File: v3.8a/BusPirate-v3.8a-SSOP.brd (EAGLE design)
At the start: 50 x 50 mm, 43 parts, among them IC1 PIC24FJ64GA002, IC3 4066, IC4 IC_FT230X-SSOP-16, J1 CON-USB-F-MINI-B

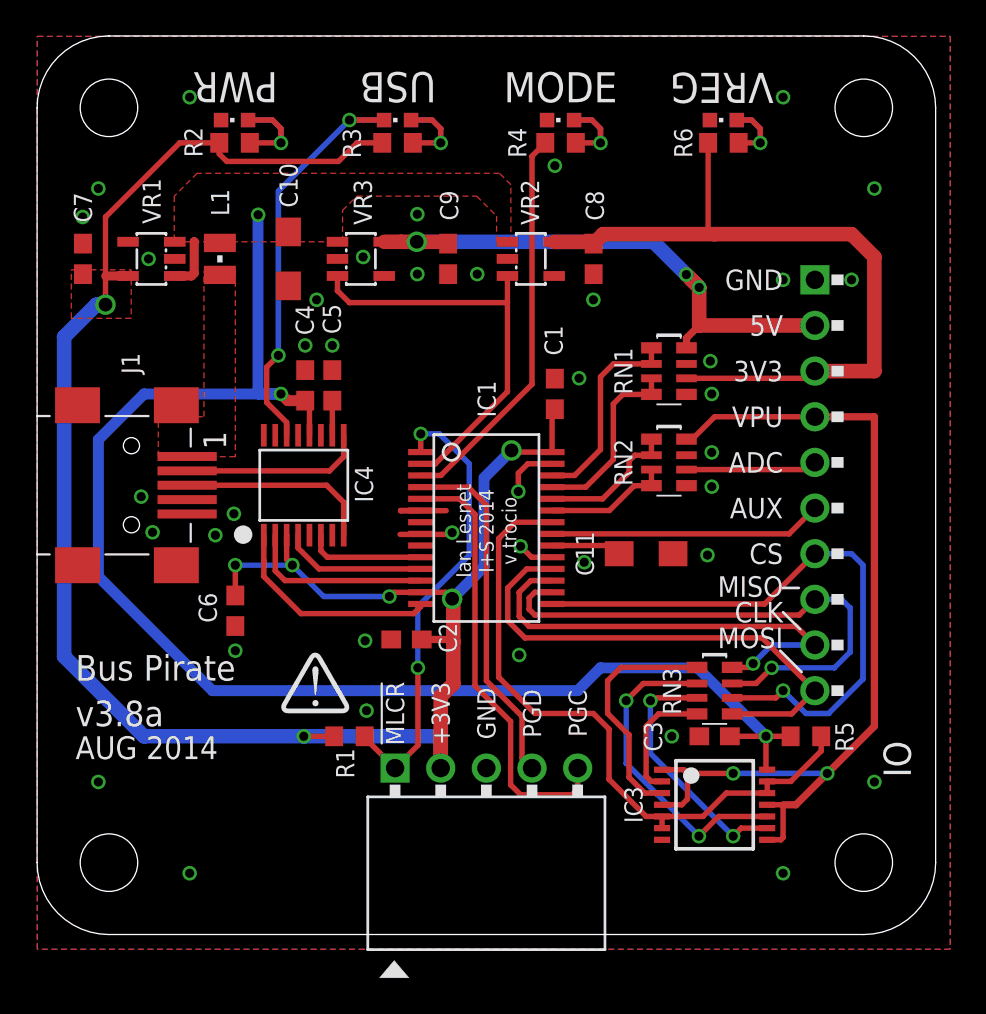
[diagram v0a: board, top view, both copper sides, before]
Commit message: -replaced SMD version for the IO and ICSP header -fixed over hang distance of header including USB connector to 1.25mm -gerber generated
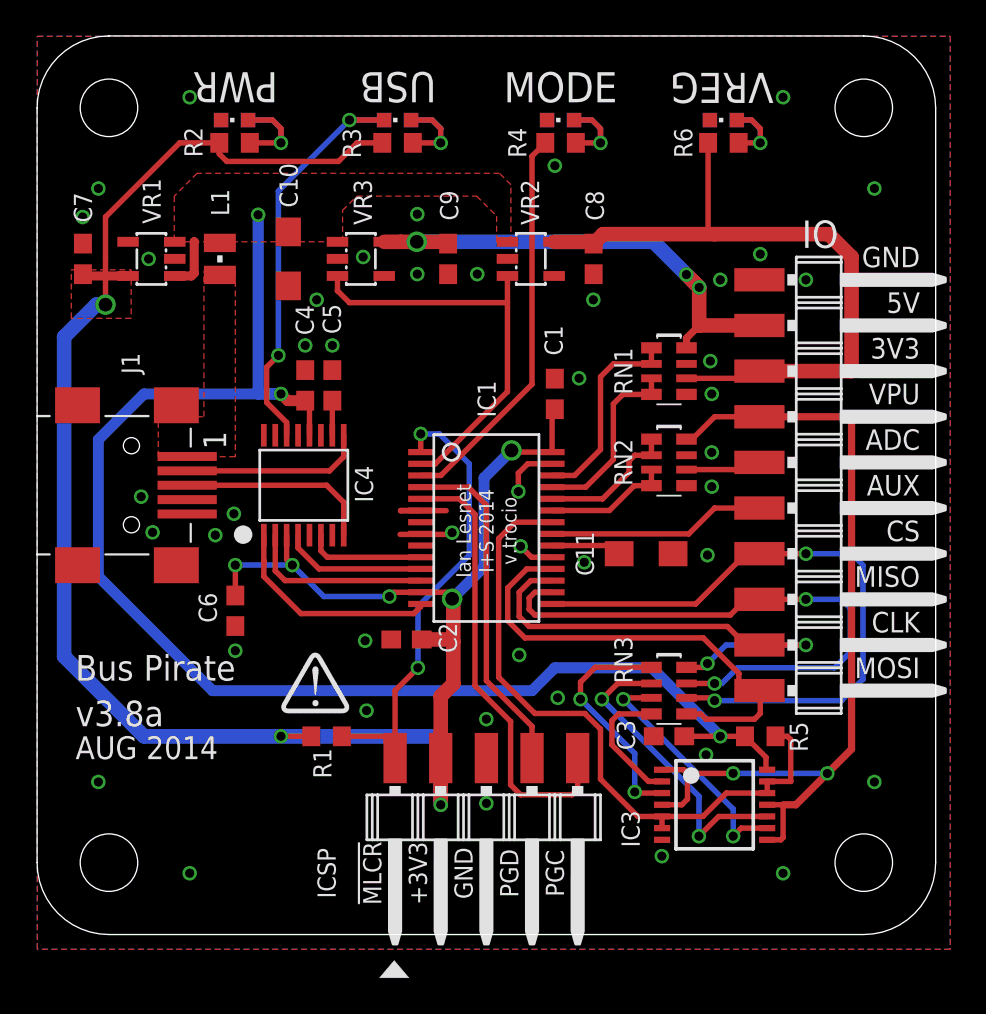
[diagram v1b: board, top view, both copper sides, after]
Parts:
- ICSP: value CON_HEADER_1X05-PTH_RIGHT_ANGLED_B -> CON_HEADER_1X05-SMD_RIGHT_ANGLED_MALE_B; device dp_devices.v6:M1X5_FEMALE_RIGHT_ANGLED_PTH_B -> dp_devices.v6:M1X5_MALE_RIGHT_ANGLED_SMD_B
- IO: value CON_HEADER_1X10-RIGHT_ANGLED_PTH -> CON_HEADER_1X10-_RIGHTANGLED_SMD; device dp_devices.v6:M1X10_FEMALE_RIGHT_ANGLED_PTH -> dp_devices.v6:M1X10_MALE_RIGHT_ANGLED_SMD
- moved IO 5.64 mm to (43.9, 25.4)
- moved ICSP 3.11 mm to (25.4, 6.92)
- moved C3 2.54 mm to (35.6, 11.4)
- moved R5 2.54 mm to (40.6, 11.4)
- moved RN3 2.54 mm to (35.6, 14.0)
- moved R1 1.27 mm to (16.5, 11.4)
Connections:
- net V+ renamed VUSB
- net VCC renamed +3V3
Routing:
- net +3V3: track 114.4 -> 120.7 mm, vias 7 -> 8
- net ADC: track 7.31 -> 4.22 mm
- net AUX1: track 15.2 -> 12.1 mm
- net SWV50: track 32.3 -> 29.2 mm
- net MISO: track 30.3 -> 32.9 mm, vias 1 -> 2
- net SWV33: track 41.0 -> 38.5 mm
- net VUSB: track 83.7 -> 81.7 mm
- net MOSI: track 28.6 -> 26.7 mm
- net VEXTERN: track 51.0 -> 49.2 mm
- net CS: track 33.8 -> 35.4 mm, vias 1 -> 2
- net CLK: track 25.7 -> 27.2 mm, vias 1 -> 2
- net MCLR: track 25.5 -> 26.7 mm
- net N$4: track 17.8 -> 17.2 mm
- net PGD: track 19.8 -> 19.2 mm
- net PGC: track 24.5 -> 25.1 mm
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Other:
- board text added: "ICSP"

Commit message: board update: -changed ICSP header to 6pins, spare pin not connected -moved all LEDs a little to the right for even space
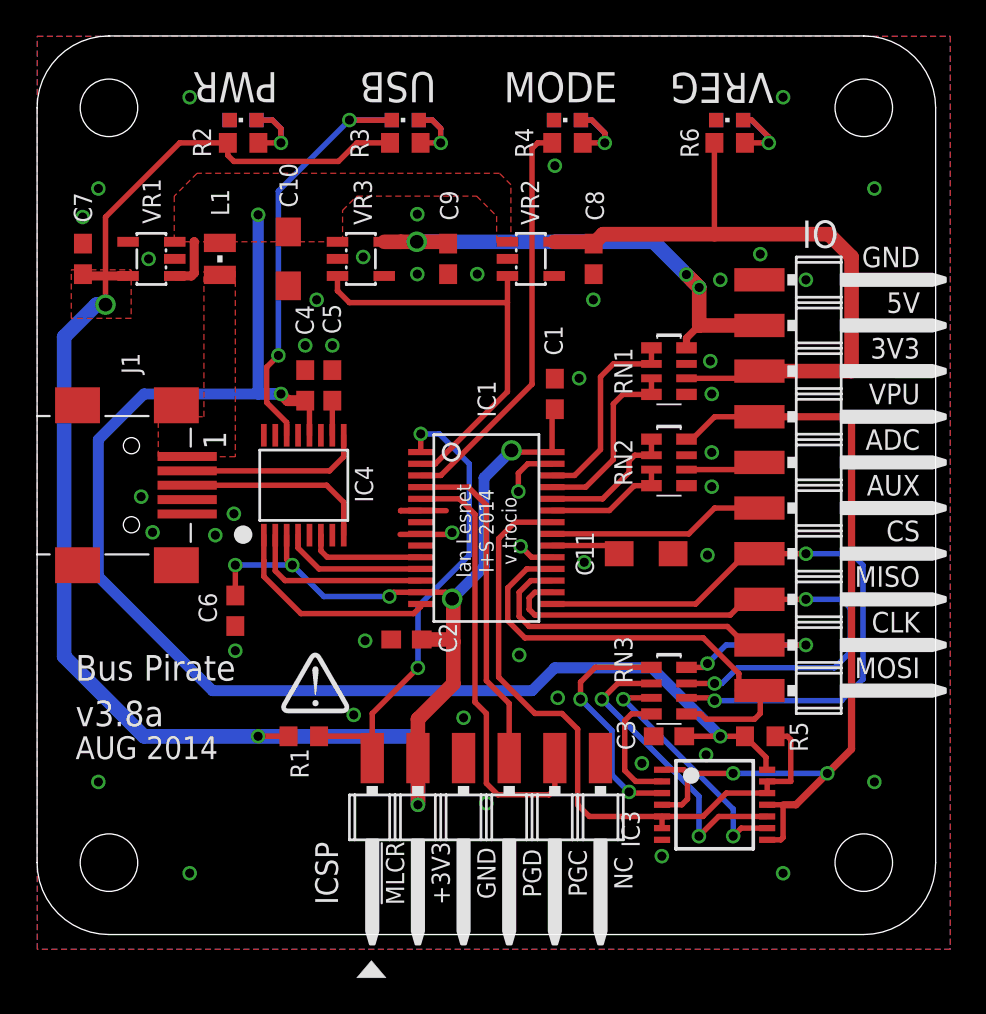
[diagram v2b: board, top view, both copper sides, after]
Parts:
- ICSP: value CON_HEADER_1X05-SMD_RIGHT_ANGLED_MALE_B -> CON_HEADER_1X06-SMD-RIGHT-ANGLED; device dp_devices.v6:M1X5_MALE_RIGHT_ANGLED_SMD_B -> dp_devices.v6:M1X6_MALE_RIGHT_ANGLED_SMD
- moved R1 1.27 mm to (15.2, 11.4)
- moved LED1 0.47 mm to (11.9, 45.7)
- moved LED1A 0.47 mm to (11.9, 45.7)
- moved R2 0.47 mm to (11.9, 44.5)
- moved LED4 0.43 mm to (20.9, 45.7)
- moved LED4A 0.43 mm to (20.9, 45.7)
- moved R3 0.43 mm to (20.9, 44.5)
- moved LED2 0.39 mm to (29.9, 45.7)
- moved LED2A 0.39 mm to (29.9, 45.7)
- moved R4 0.39 mm to (29.9, 44.5)
- moved LED3 0.35 mm to (38.9, 45.7)
- moved LED3A 0.35 mm to (38.9, 45.7)
- moved R6 0.35 mm to (38.9, 44.5)
- turned ICSP to 180 degrees
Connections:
- net +3V3: now also ICSP.5; no longer ICSP.2
- net GND: now also ICSP.4; no longer ICSP.3
- net MCLR: now also ICSP.6; no longer ICSP.1
- net PGC: now also ICSP.2; no longer ICSP.5
- net PGD: now also ICSP.3; no longer ICSP.4
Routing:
- net N$7: track 7.38 -> 5.95 mm
- net N$13: track 6.84 -> 5.55 mm
- net RXLED: track 23.8 -> 24.6 mm
- net PULLUPEN: track 37.2 -> 38.1 mm
- net N$6: track 6.30 -> 5.58 mm
- net MCLR: track 26.7 -> 26.0 mm
- net LD1: track 22.0 -> 22.7 mm
- net N$1: track 7.34 -> 6.74 mm
- net PGD: track 19.2 -> 18.7 mm
- net PGC: track 25.1 -> 24.5 mm
- net GND: vias 45 -> 46
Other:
- board text added: "NC"
